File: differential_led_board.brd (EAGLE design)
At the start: 72.1 x 117 mm, 59 parts, among them IC1 SN75175, IC10 TJA1057, IC2 TLV803, IC3 LD1117S33, IC4 74LVC1G157, IC5 74LVC1G157, IC6 CD40109B, IC7 STM32F042F, IC8 AT25SF041, IC9 LT6100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

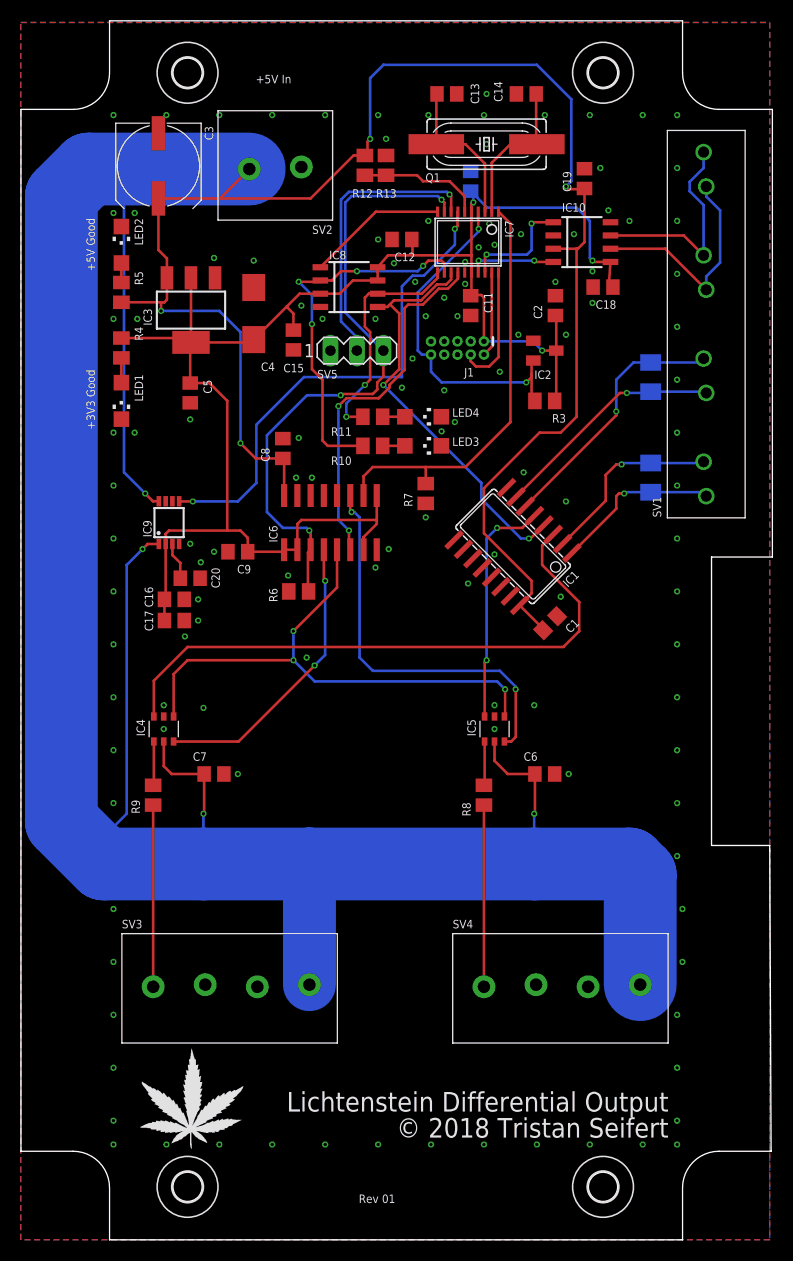
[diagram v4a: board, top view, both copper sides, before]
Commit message: rev2 of differential output board (fix capacitor footprint)
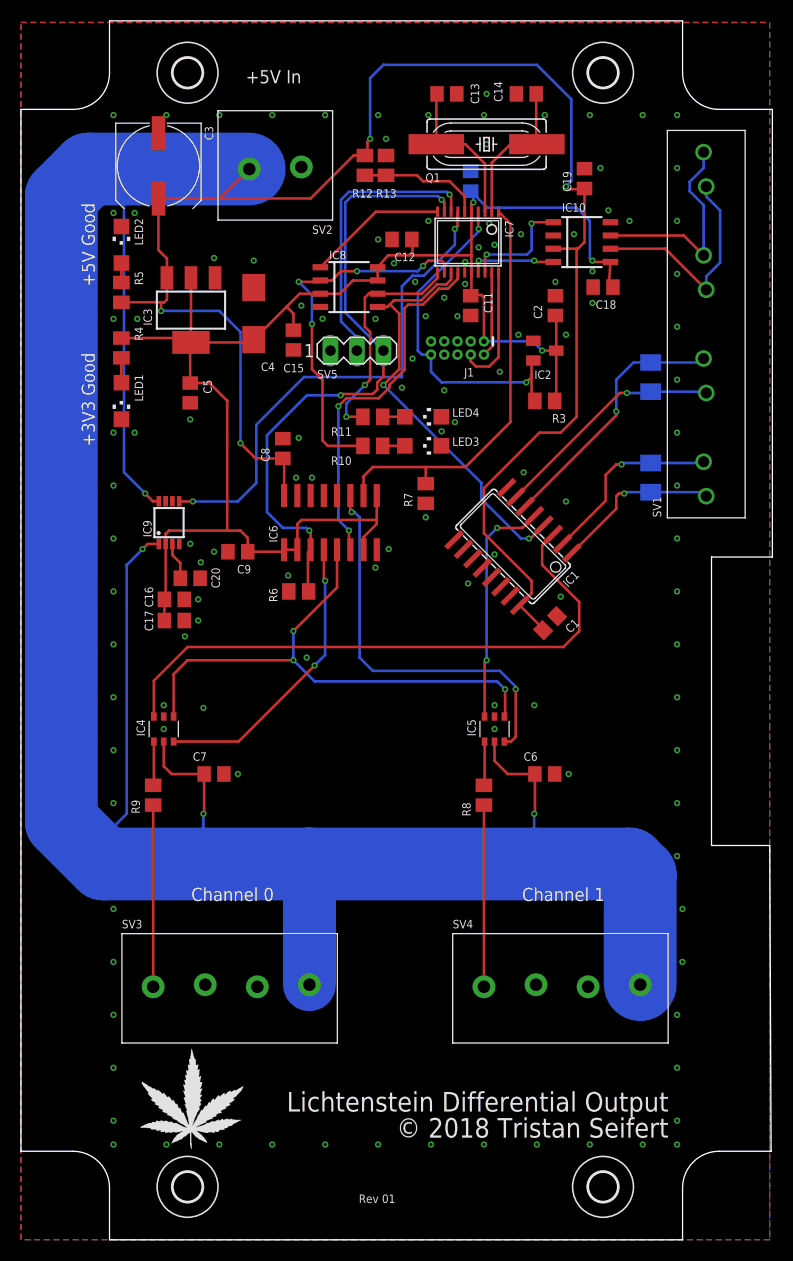
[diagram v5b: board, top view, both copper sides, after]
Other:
- board text added: "Channel 0"
- board text added: "Channel 1"
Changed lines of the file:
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@@
 <text x="62.168690625" y="9.8044" size="1.8796" layer="25" font="vector" ratio="10" distance="33" align="bottom-right">Lichtenstein Differential Output
 © 2018 Tristan Seifert</text>
-<text x="24.257" y="110.998" size="0.8128" layer="25" font="vector" ratio="10" align="bottom-center">+5V In</text>
-<text x="7.112" y="95.504" size="0.8128" layer="25" font="vector" ratio="10" rot="R90" align="bottom-center">+5V Good</text>
-<text x="7.112" y="80.645" size="0.8128" layer="25" font="vector" ratio="10" rot="R90" align="bottom-center">+3V3 Good</text>
+<text x="24.257" y="110.998" size="1.27" layer="25" font="vector" ratio="10" align="bottom-center">+5V In</text>
+<text x="7.112" y="95.504" size="1.27" layer="25" font="vector" ratio="10" rot="R90" align="bottom-center">+5V Good</text>
+<text x="7.112" y="80.645" size="1.27" layer="25" font="vector" ratio="10" rot="R90" align="bottom-center">+3V3 Good</text>
 <text x="32.4358" y="3.5306" size="0.8128" layer="25" font="vector" ratio="10">Rev 01</text>
+<text x="20.32" y="32.512" size="1.27" layer="25" font="vector" ratio="10" align="bottom-center">Channel 0</text>
+<text x="52.07" y="32.512" size="1.27" layer="25" font="vector" ratio="10" align="bottom-center">Channel 1</text>
 </plain>
 <attributes>
@@
 <attribute name="MOUSER" value="595-TLV803SDBZR" x="50.292" y="85.344" size="0.8128" layer="27" font="vector" ratio="10" rot="R270" display="off"/>
 <attribute name="NAME" x="50.927" y="83.439" size="0.8128" layer="25" ratio="10" rot="R180"/>
-<attribute name="VALUE" x="47.117" y="87.249" size="1.27" layer="27" rot="R270"/>
 </element>
 <element name="C2" library="rcl" library_urn="urn:adsk.eagle:library:334" package="C0805" package3d_urn="urn:adsk.eagle:package:23617/2" value="100nF" x="51.308" y="89.662" smashed="yes" rot="R90">
